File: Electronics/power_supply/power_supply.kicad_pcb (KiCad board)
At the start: 2 copper layers, 56.5 x 57.5 mm, 74 parts, among them IC2 LM5069MMX-2_NOPB, J1 Conn_01x02_Male, J10 9801-0-15-15-23-27-10-0, J11 22-03-5035, J12 9801-0-15-15-23-27-10-0, J13 9801-0-15-15-23-27-10-0, J14 9801-0-15-15-23-27-10-0, J2 9801-0-15-15-23-27-10-0, J3 Conn_01x02_Male, J5 9801-0-15-15-23-27-10-0, J6 Conn_01x04_Male, J7 Conn_01x02_Male, J8 22-03-5035, Q1 IPD90N04S4L04ATMA1, Q2 PNP, U1 R-78B1.5-2.0, U2 INA226, U3 INA226

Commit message: Update PowerSupply PCB
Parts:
- removed C18, C4: 10uF, Capacitor_SMD:C_1206_3216Metric_Pad1.33x1.80mm_HandSolder
- removed C19, C5: 22uF, Capacitor_SMD:C_1206_3216Metric_Pad1.33x1.80mm_HandSolder
- removed H1, H2: MountingHole, MountingHole:MountingHole_3.2mm_M3
- removed J11, J8: 22-03-5035, MiAM:SHDR3W60P0X250_1X3_990X490X590P
- removed Q2: PNP, Package_TO_SOT_SMD:SOT-1123
- added D2: LED, LED_SMD:LED_0805_2012Metric_Pad1.15x1.40mm_HandSolder, F.Cu at (143.8, 54.9)
- added H5: 9774030951R, MiAM:9774030951R, F.Cu at (115.8, 50.9)
- added H6: 9774030951R, MiAM:9774030951R, F.Cu at (164.8, 50.9)
- added J4: 821-22-002-10-000101, MiAM:8212200210000101, B.Cu at (121.8, 51.8)
- added NT1: NetTie_2, NetTie:NetTie-2_SMD_Pad0.5mm, B.Cu at (158.9, 103.5)
- added Q3: BC857, Package_TO_SOT_SMD:SOT-23, F.Cu at (167.1, 86.9)
- added R11: R, Resistor_SMD:R_0805_2012Metric, F.Cu at (147.5, 54.9)
- C24, D5, JP1, JP2, R9: moved to B.Cu
- R7: value 6k -> 5k
- moved C17 100.4 mm to (166.4, 61.9), turned to 90 degrees
- moved RV1 82.8 mm to (165.3, 57.2), turned to 90 degrees
- moved C12 76.0 mm to (141.3, 62.1), turned to -90 degrees
- moved R3 73.7 mm to (160.1, 55.8)
- moved C10 73.2 mm to (154.8, 54.9)
- moved R4 65.0 mm to (151.1, 54.9), turned to 180 degrees
- moved JP2 63.3 mm to (144.7, 62.0), turned to 90 degrees
- moved RV2 61.8 mm to (139.2, 57.2), turned to 180 degrees
- moved R2 60.7 mm to (123.3, 54.9), turned to 180 degrees
- moved C24 58.8 mm to (140.0, 62.8), turned to 90 degrees
- moved D6 57.3 mm to (127.0, 54.9), turned to 180 degrees
- moved R1 55.2 mm to (140.0, 69.5), turned to -90 degrees
- moved R7 50.7 mm to (134.7, 54.8), turned to 180 degrees
- moved JP1 50.0 mm to (127.0, 62.6), turned to 90 degrees
- moved C11 39.0 mm to (139.9, 91.9), turned to 180 degrees
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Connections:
- net Net-(D4-K) renamed /Vbat
- C25 pad 2: GND -> GNDS
- C29 pad 2: GND -> GNDS
- D6 pad 1: unconnected-(D6-K-Pad1) -> GND
- D6 pad 2: unconnected-(D6-A-Pad2) -> Net-(D6-A)
- IC2 pad 4: GND -> GNDS
- IC2 pad 5: GND -> GNDS
- R10 pad 2: GND -> GNDS
- R2 pad 1: Net-(D2-A) -> Net-(D6-A)
- R8 pad 1: VS -> Net-(IC2-SENSE)
- R8 pad 2: VS -> Net-(Q1-D)
- R8 pad 3: Net-(Q1-D) -> VS
- R8 pad 4: Net-(IC2-SENSE) -> VS
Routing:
- net GND: track 0.00 -> 110.9 mm, vias 0 -> 52
- net /SDA: track 0.00 -> 70.7 mm, vias 0 -> 3
- net +3.3V: track 0.00 -> 68.9 mm, vias 0 -> 3
- net /SCL: track 0.00 -> 67.3 mm, vias 0 -> 3
- net +24V: track 0.00 -> 49.6 mm, vias 0 -> 20
- net /Vtrim: track 0.00 -> 26.8 mm, vias 0 -> 3
- net Net-(R4-Pad1): track 0.00 -> 18.0 mm, vias 0 -> 2
- net /Gate: track 0.00 -> 18.0 mm, vias 0 -> 2
- net +7.5V: track 0.00 -> 16.8 mm, vias 0 -> 3
- net /Vtrim12: track 0.00 -> 15.3 mm, vias 0 -> 2
- net Net-(IC2-TIMER): track 0.00 -> 11.8 mm
- net +5V: track 0.00 -> 11.7 mm, vias 0 -> 4
- net /Vout12: track 0.00 -> 9.72 mm
- net Net-(C10-Pad1): track 0.00 -> 9.45 mm, vias 0 -> 2
- net Net-(C24-Pad1): track 0.00 -> 9.30 mm, vias 0 -> 1
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- added copper zone on F.Cu, net +12V
- added copper zone on F.Cu, net +24V
- added copper zone on In2.Cu, net +24V
- added copper zone on In2.Cu, net +5V
- added copper zone on F.Cu, net +7.5V
- added copper zone on In1.Cu, net /Vbat
- added copper zone on F.Cu, net /Vout
- added copper zone on F.Cu, net /Vout12
- added copper zone on B.Cu, net GND
- added copper zone on B.Cu, net GNDS
- added copper zone on F.Cu, net VS
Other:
- board size 56.5 x 57.5 mm -> 58 x 58 mm
- copper layers 2 -> 4

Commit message: Update main robot PCB
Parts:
- moved C11 2.51 mm to (142.4, 92.2), turned to 0 degrees
- moved C9 0.36 mm to (164.5, 65.4)
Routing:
- net +24V: track 49.6 -> 51.1 mm, vias 20 -> 19
- net GND: track 110.9 -> 109.4 mm, vias 52 -> 50

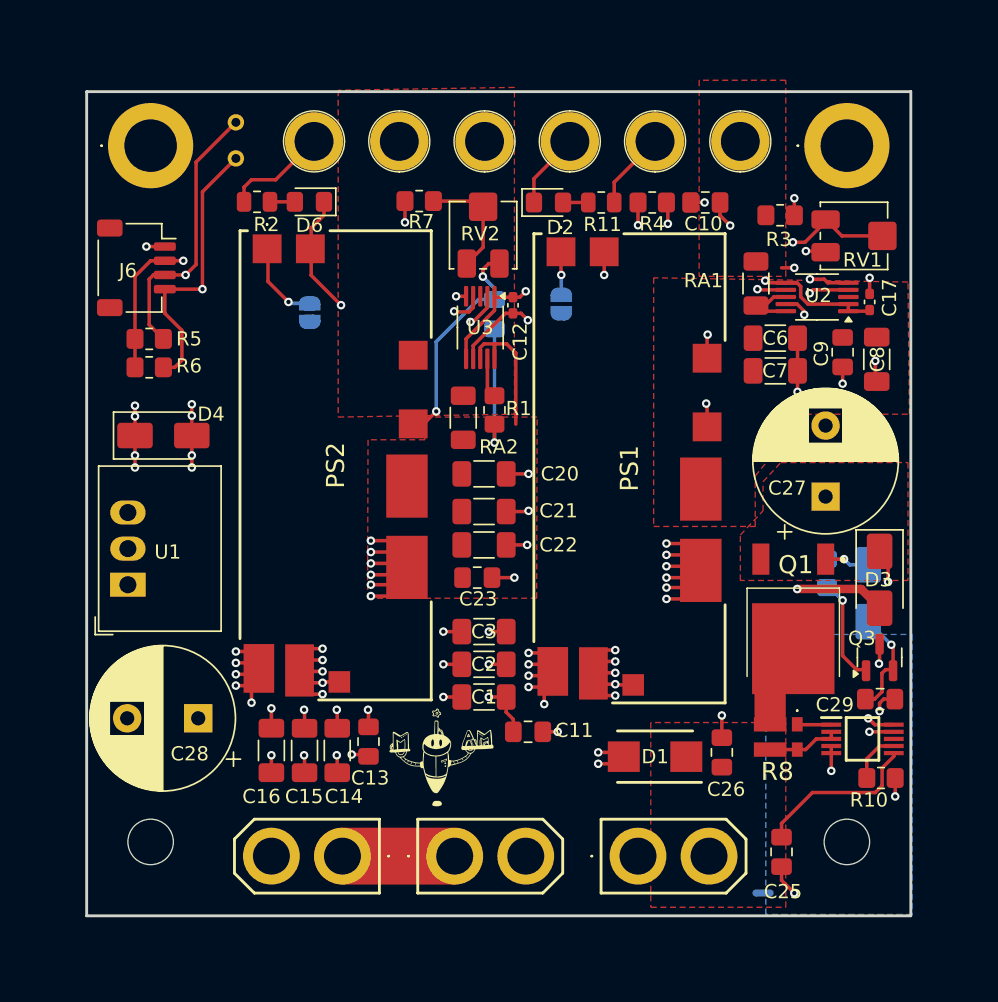
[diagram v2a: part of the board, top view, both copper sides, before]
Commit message: PCB update - passes DRC
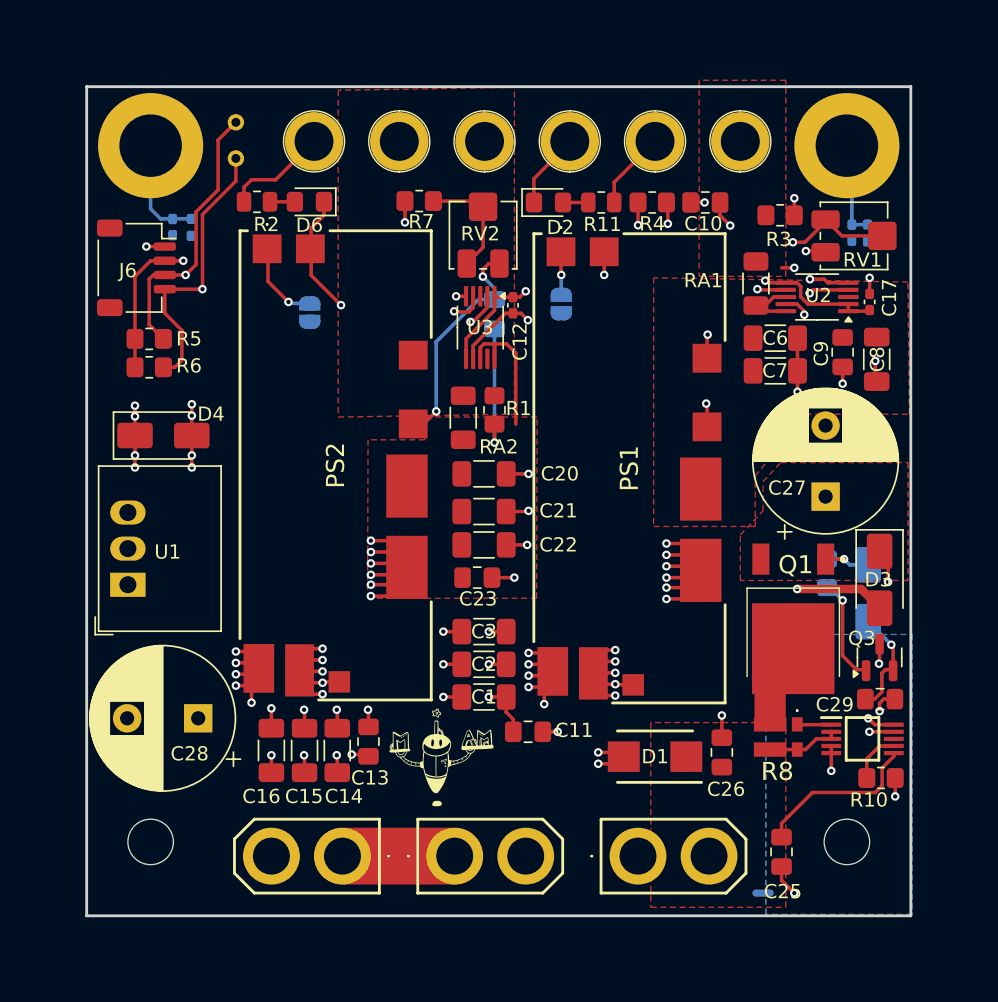
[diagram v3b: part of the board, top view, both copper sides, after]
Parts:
- added C4: 10nF, Capacitor_SMD:C_0402_1005Metric_Pad0.74x0.62mm_HandSolder, B.Cu at (117.3, 56.6)
- added C5: 10nF, Capacitor_SMD:C_0402_1005Metric_Pad0.74x0.62mm_HandSolder, B.Cu at (165.2, 57.0)
- added R12: 100k, Resistor_SMD:R_0402_1005Metric_Pad0.72x0.64mm_HandSolder, B.Cu at (118.7, 56.7)
- added R13: 100k, Resistor_SMD:R_0402_1005Metric_Pad0.72x0.64mm_HandSolder, B.Cu at (166.2, 57.0)
- H5, H6: value 9774030951R -> 9774030360R; footprint MiAM:9774030951R -> MiAM:9774030360R
- moved H5 49.0 mm to (164.8, 50.9)
- moved H6 49.0 mm to (115.8, 50.9)
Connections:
- H5 pad 1: unconnected-(H5-Pad1) -> Net-(C5-Pad1)
- H6 pad 1: unconnected-(H6-Pad1) -> Net-(C4-Pad1)
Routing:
- net Net-(C4-Pad1): track 0.00 -> 7.59 mm
- net Net-(C5-Pad1): track 0.00 -> 6.30 mm
- net +12V: track 2.81 -> 0.71 mm
- added copper zone on In1.Cu, net GND
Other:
- board size 58 x 58 mm -> 58 x 58.3 mm

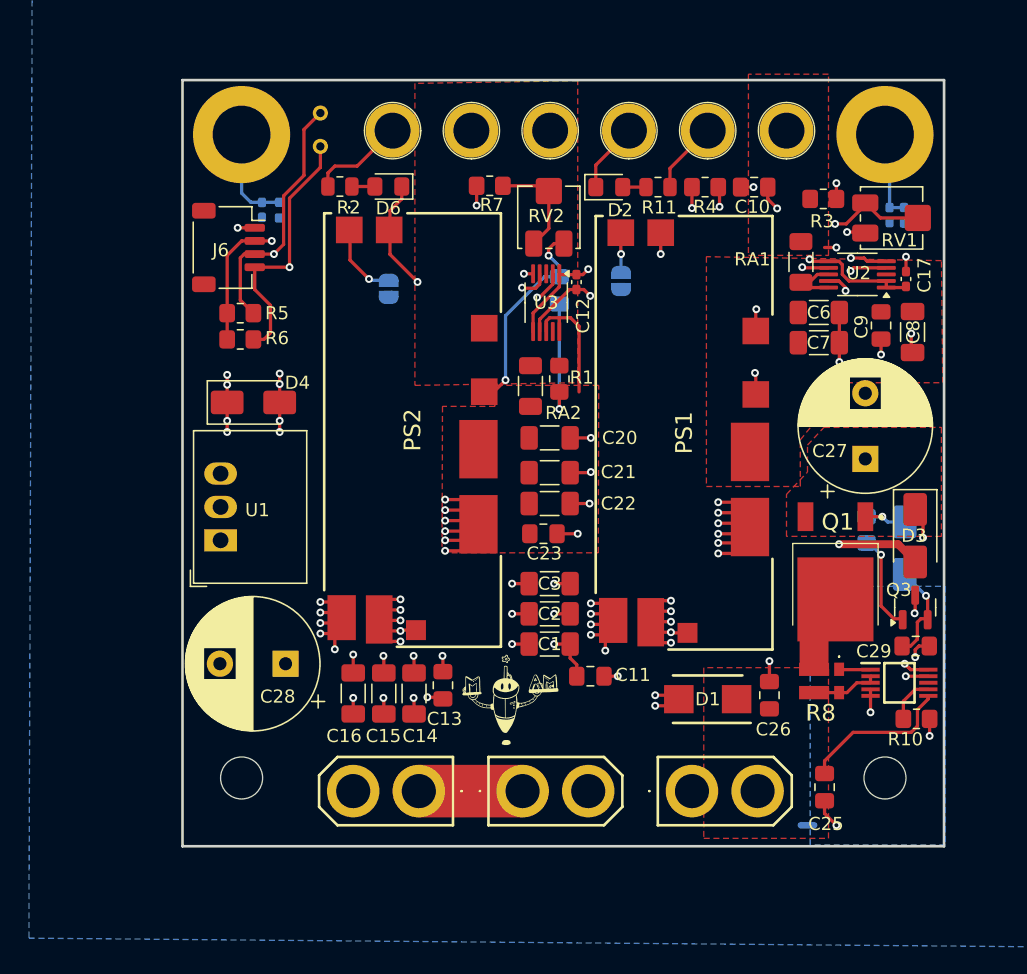
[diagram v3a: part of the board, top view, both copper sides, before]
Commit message: [Elec] V2 of power supply
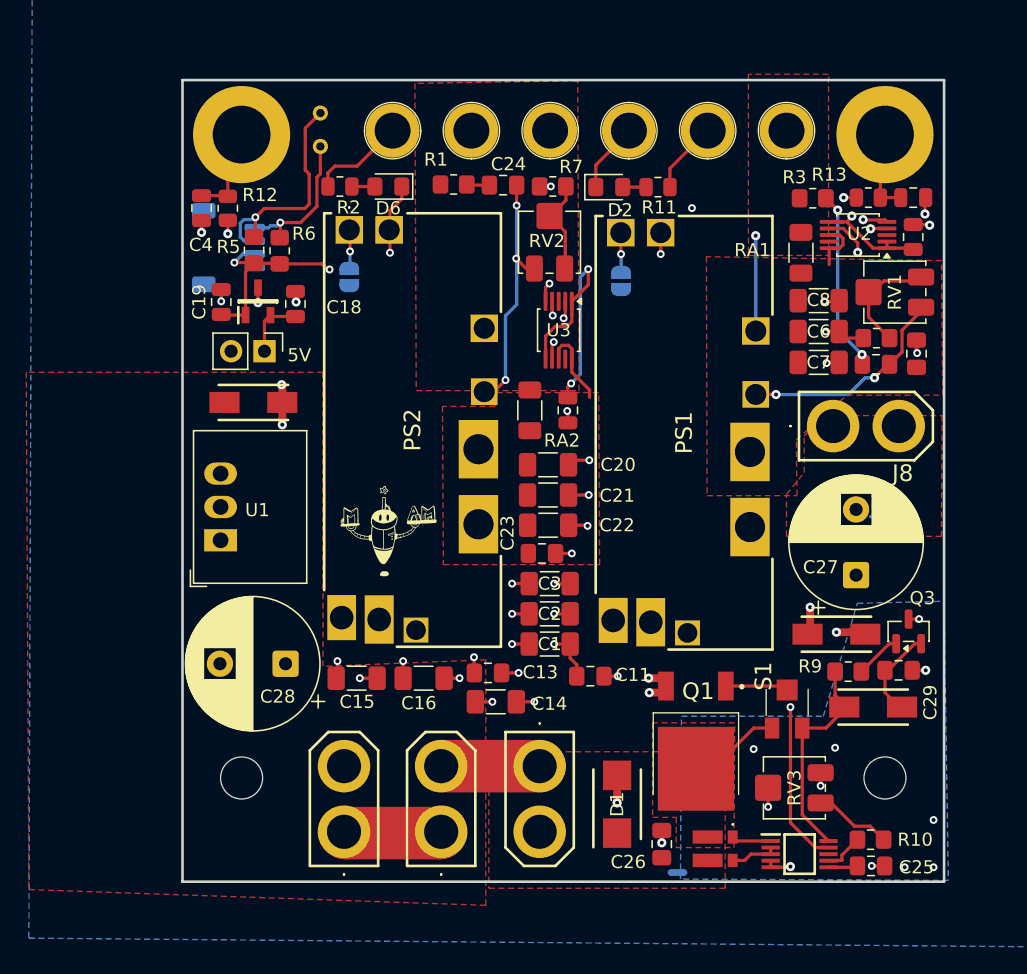
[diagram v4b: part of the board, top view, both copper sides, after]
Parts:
- added C18: 0.1uF, Capacitor_SMD:C_0805_2012Metric, F.Cu at (119.9, 63.8)
- added C19: 0.1uF, Capacitor_SMD:C_0805_2012Metric, F.Cu at (114.2, 63.6)
- added IC1: TLV76033DBZR, MiAM:SOT95P237X112-3N, F.Cu at (117.0, 63.6)
- added J8: Conn_01x02_Male, MiAM:XT30UM, F.Cu at (160.8, 73.1)
- added J9: Conn_01x02_Pin, Connector_PinHeader_2.54mm:PinHeader_1x02_P2.54mm_Vertical, F.Cu at (117.5, 67.4)
- added RV3: 3314J-2-104E, Potentiometer_SMD:Potentiometer_Bourns_3314J_Vertical, F.Cu at (157.9, 100.7)
- added S1: 7813J-1-051E, MiAM:7813J1051E, F.Cu at (157.3, 94.7)
- C11, C13, C23, C25, C9: value 0.047uF -> 47nF
- C12, C17: footprint Capacitor_SMD:C_0402_1005Metric_Pad0.74x0.62mm_HandSolder -> Capacitor_SMD:C_0805_2012Metric
- C24, R9: moved to F.Cu
- C4, C5: footprint Capacitor_SMD:C_0402_1005Metric_Pad0.74x0.62mm_HandSolder -> Capacitor_SMD:C_0805_2012Metric; moved to F.Cu
- D3, D4: value CMSH3-60MA TR13 PBFREE -> SS14; footprint Diode_SMD:D_SMA -> MiAM:DIONM5327X242N
- D5: value CMSH3-60MA TR13 PBFREE -> SS14; footprint Diode_SMD:D_SMA -> MiAM:DIONM5327X242N; moved to F.Cu
- J4: value 821-22-002-10-000101 -> 821-22-002-10-001101
- J6: moved to B.Cu
- PS1, PS2: footprint MiAM:APXW012A0X3SRDZ -> MiAM:APXW012A0X3SRDZ_TH
- R10: value 132k -> 100k
- R11, R2: value R -> 5k
- R12, R13: footprint Resistor_SMD:R_0402_1005Metric_Pad0.72x0.64mm_HandSolder -> Resistor_SMD:R_0805_2012Metric; moved to F.Cu
- RV1: value 10k -> 652-3314J-2-103E
- RV2: value 10k -> 3314J-2-103E
- U1: value R-78B1.5-2.0 -> R-78B5.0-2.0
- moved R4 17.4 mm to (164.2, 66.4)
- moved R1 16.8 mm to (131.9, 54.7), turned to 0 degrees
- moved Q1 16.7 mm to (150.4, 96.0)
- moved C10 16.4 mm to (164.1, 68.4)
- moved R8 15.1 mm to (151.9, 105.3)
- moved IC2 15.1 mm to (158.3, 105.7)
- moved C26 14.0 mm to (147.8, 104.9)
- moved D5 12.3 mm to (163.9, 94.5), turned to 180 degrees
- moved J7 11.8 mm to (138.5, 99.0), turned to -90 degrees
- moved R9 10.9 mm to (162.0, 91.8), turned to 0 degrees
- moved D1 10.6 mm to (144.4, 101.9), turned to 90 degrees
- moved NT1 10.5 mm to (149.0, 107.1)
- moved R10 9.84 mm to (163.7, 104.6)
- moved C12 9.79 mm to (140.7, 71.9)
- moved D3 9.60 mm to (161.1, 89.0), turned to 0 degrees
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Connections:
- IC2 pad 2: VS -> Net-(IC2-UVLO)
- IC2 pad 3: VS -> Net-(IC2-UVLO)
- Q1 pad 1: /Gate -> Net-(Q1-G)
- R10 pad 2: GNDS -> Net-(R10-Pad2)
- R8 pad 4: VS -> Net-(IC2-UVLO)
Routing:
- net GND: track 109.2 -> 57.3 mm, vias 50 -> 35
- net +24V: track 51.1 -> 33.6 mm, vias 19 -> 11
- net +3.3V: track 69.0 -> 84.8 mm, vias 3 -> 5
- net /Vtrim: track 26.8 -> 16.1 mm, vias 3 -> 2
- net Net-(R4-Pad1): track 18.0 -> 8.21 mm, vias 2 -> 0
- net Net-(IC2-TIMER): track 11.8 -> 2.10 mm
- net +7.5V: track 16.8 -> 7.26 mm, vias 3 -> 1
- net Net-(C24-Pad1): track 9.30 -> 1.68 mm, vias 1 -> 0
- net Net-(R10-Pad2): track 0.00 -> 5.16 mm
- net VS: track 4.94 -> 0.00 mm
- net Net-(Q1-G): track 0.00 -> 4.37 mm
- net Net-(C10-Pad1): track 9.45 -> 13.8 mm
- net Net-(Q3-B): track 7.23 -> 3.53 mm, vias 1 -> 0
- net Net-(IC2-UVLO): track 0.00 -> 3.60 mm
- net /Vout12: track 9.72 -> 6.26 mm
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- added copper zone on F.Cu, net /Vbat
- added copper zone on In1.Cu, net GNDS
- added copper zone on In2.Cu, net GNDS
- added copper zone on F.Cu, net Net-(Q1-D)
- removed copper zone on In1.Cu, net /Vbat
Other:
- board size 58 x 58.3 mm -> 58 x 61 mm
- board text added: "5V"

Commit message: PCB fixup
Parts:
- added C30: 0.1uF 50V, Capacitor_SMD:C_0402_1005Metric_Pad0.74x0.62mm_HandSolder, F.Cu at (155.1, 105.2)
- Q3: value BC857 -> MMBT5401
- R4: value 6k -> 6.8k
- R7: value 5k -> 4.7k
- moved R10 0.40 mm to (164.1, 104.6)
- moved IC2 0.40 mm to (158.7, 105.7)
- moved C25 0.36 mm to (164.1, 106.6)
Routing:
- net GND: track 57.3 -> 59.8 mm, vias 35 -> 54
- net Net-(C10-Pad1): track 13.8 -> 15.1 mm
- net +24V: track 33.6 -> 34.7 mm
- net /SDA: track 72.4 -> 73.4 mm

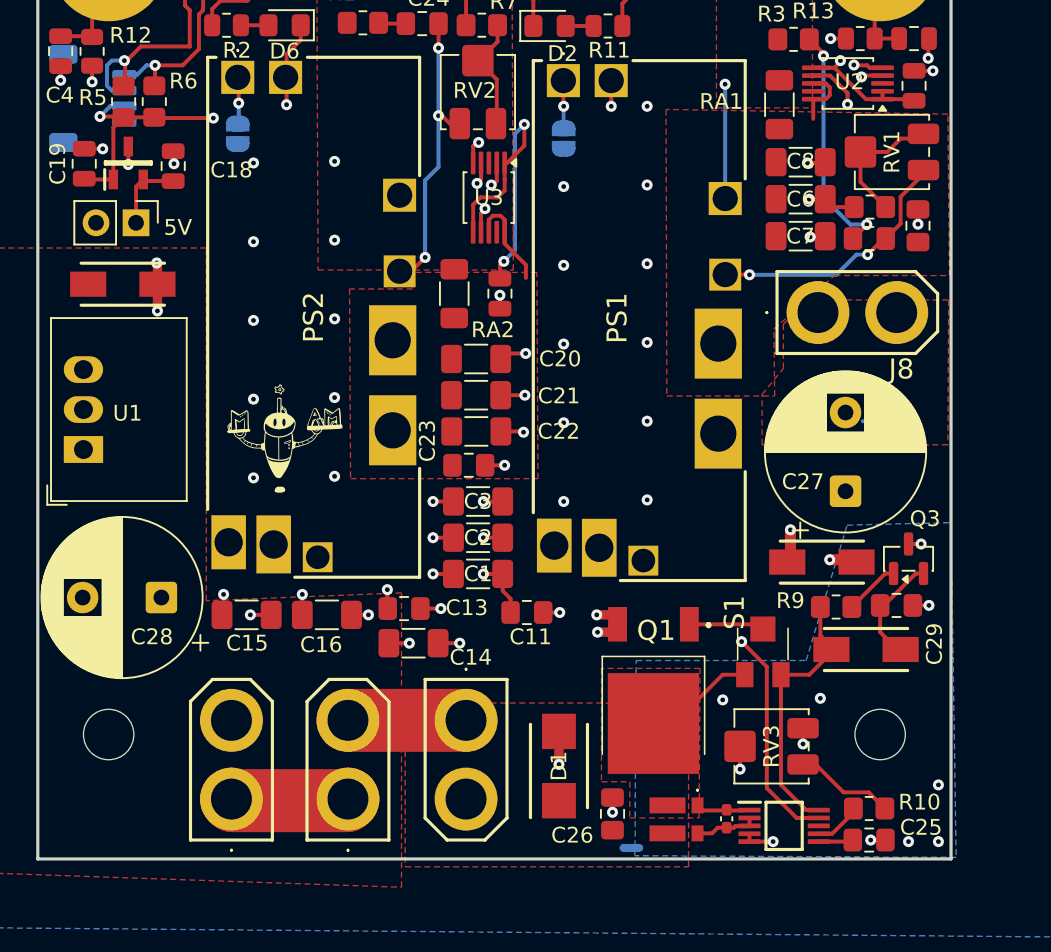
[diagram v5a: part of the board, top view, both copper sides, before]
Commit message: Add main PCB for 2026
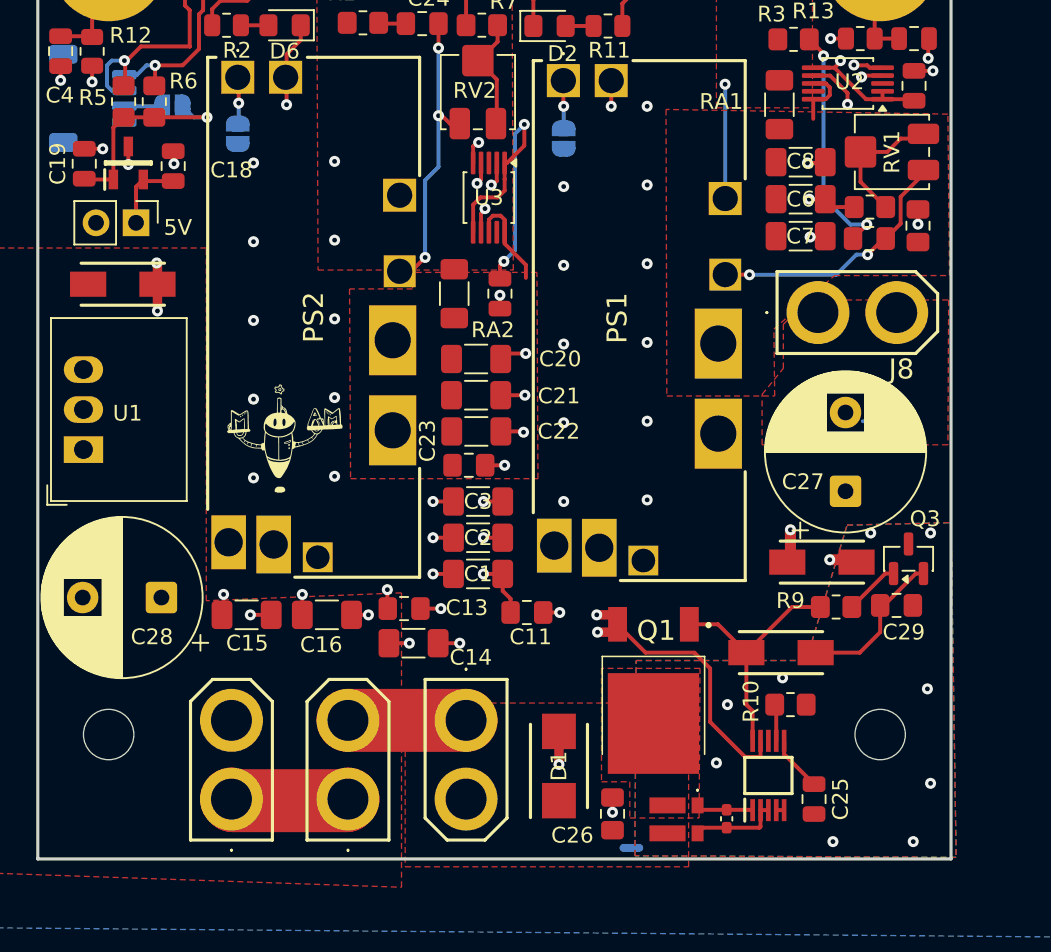
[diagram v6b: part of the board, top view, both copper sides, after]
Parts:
- removed RV3: 3314J-2-104E, Potentiometer_SMD:Potentiometer_Bourns_3314J_Vertical
- removed S1: 7813J-1-051E, MiAM:7813J1051E
- added JP3: SolderJumper_2_Open, Jumper:SolderJumper-2_P1.3mm_Open_RoundedPad1.0x1.5mm, B.Cu at (119.8, 60.0)
- C25: value 47nF -> 0.1uF; footprint Capacitor_SMD:C_0805_2012Metric_Pad1.18x1.45mm_HandSolder -> Capacitor_SMD:C_0805_2012Metric
- R10: value 100k -> 20k
- R11, R2: value 5k -> 30k
- moved R10 8.28 mm to (159.1, 98.0)
- moved D5 5.40 mm to (158.5, 94.7)
- moved C25 4.36 mm to (160.6, 104.0), turned to -90 degrees
- moved IC2 3.35 mm to (157.7, 102.5), turned to 90 degrees
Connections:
- J6 pad 2: +3.3V -> Net-(J6-Pin_2)
- Q1 pad 1: Net-(Q1-G) -> /Gate
- R10 pad 2: Net-(R10-Pad2) -> GNDS
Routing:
- net GNDS: track 6.85 -> 0.50 mm, vias 11 -> 9
- net Net-(Q1-D): track 5.78 -> 0.00 mm
- net Net-(R10-Pad2): track 5.56 -> 0.00 mm
- net Net-(Q1-G): track 4.37 -> 0.00 mm
- net Net-(D5-K): track 6.60 -> 9.69 mm
- net Net-(J6-Pin_2): track 0.00 -> 1.95 mm
- net +24V: track 34.7 -> 36.6 mm, vias 11 -> 10
- net Net-(IC2-UVLO): track 4.01 -> 5.73 mm
- net +3.3V: track 84.9 -> 83.4 mm, vias 5 -> 4
- net Net-(IC2-TIMER): track 2.46 -> 3.54 mm
- net /Gate: track 16.8 -> 16.0 mm
- net Net-(IC2-SENSE): track 3.01 -> 3.72 mm
- net Net-(IC2-PWR): track 2.84 -> 2.34 mm
- added copper zone on F.Cu, net GNDS
